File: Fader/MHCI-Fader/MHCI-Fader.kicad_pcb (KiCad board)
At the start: 2 copper layers, 1 part

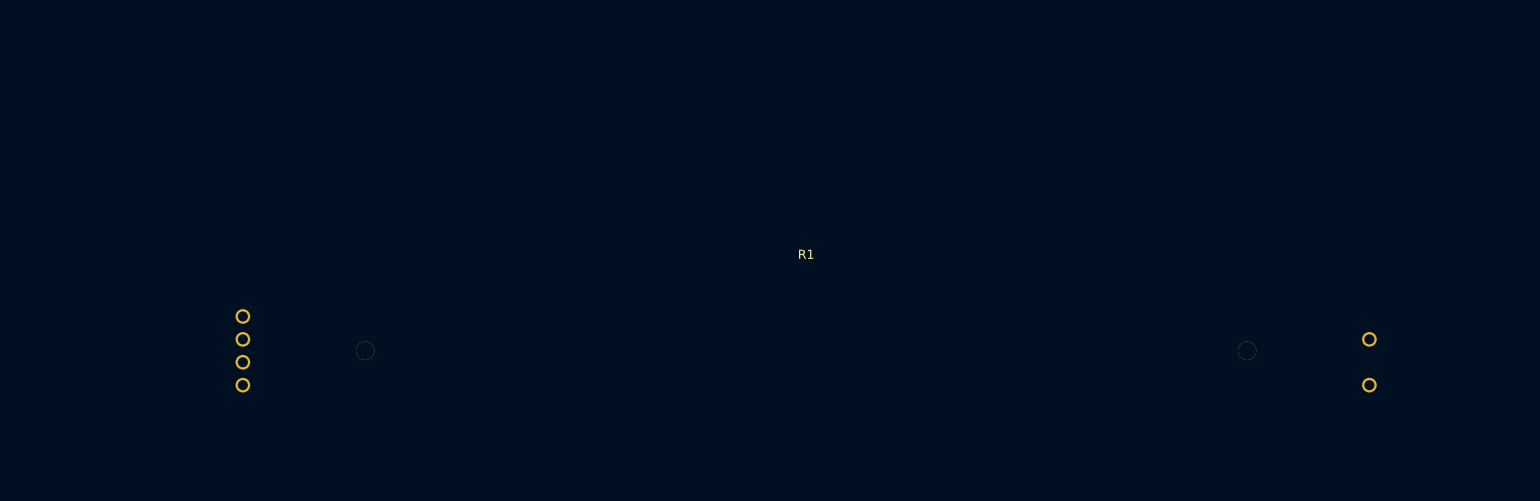
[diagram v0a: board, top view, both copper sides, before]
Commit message: Add all Waveshare footprints
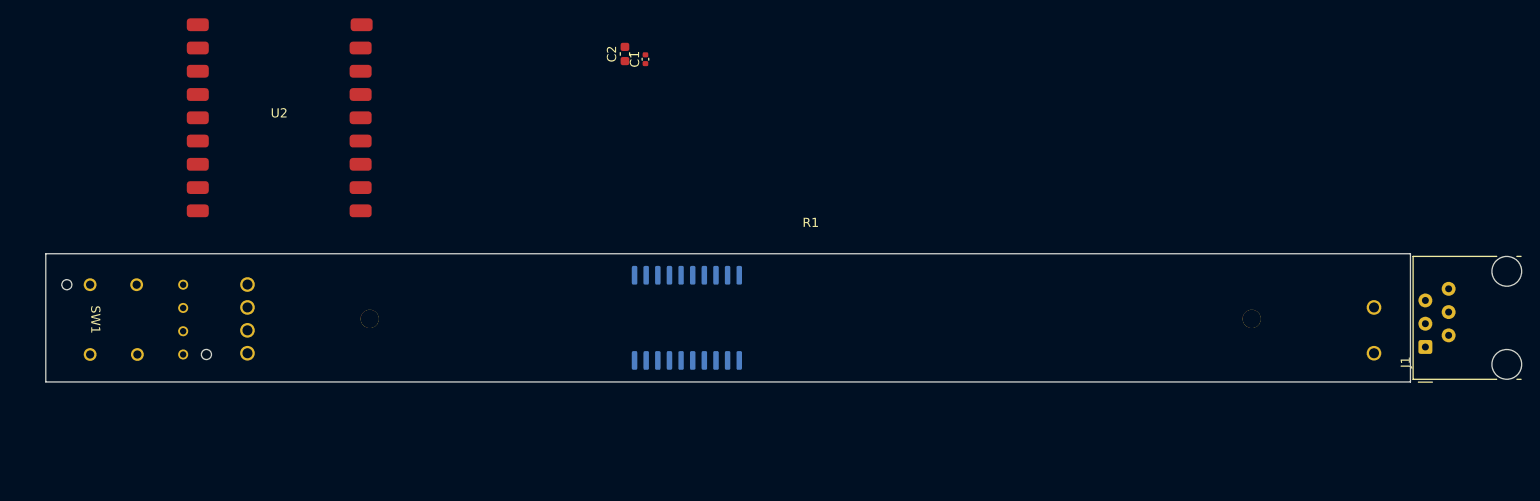
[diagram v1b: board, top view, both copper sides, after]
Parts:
- added C1: 1uF, Capacitor_SMD:C_0402_1005Metric, F.Cu at (128.5, 73.8)
- added C2: 10u, Capacitor_SMD:C_0603_1608Metric, F.Cu at (126.2, 73.2)
- added J1: RJ12, Connector_RJ:RJ12_Amphenol_54601-x06_Horizontal, F.Cu at (213.6, 105.2)
- added SW1: SW_Push_LED, MCHI:SP86N_AB Switch, F.Cu at (72.9, 102.2)
- added U1: ISOW1044, Package_SO:SOIC-20W_7.5x12.8mm_P1.27mm, B.Cu at (133.0, 102.0)
- added U2: ~, MCHI:ESP-32-S3-Zero - SMD, F.Cu at (88.5, 80.2)
- moved R1 3.52 mm to (146.5, 92.1)
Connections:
- R1 pad 1: unconnected-(R1-Pad1) -> +3V3
- R1 pad 2: unconnected-(R1-Pad2) -> Net-(R1-Pad2)
- R1 pad 3: unconnected-(R1-Pad3) -> GND
- R1 pad 4: unconnected-(R1-K-Pad4) -> POT_LED
- R1 pad 5: unconnected-(R1-A-Pad5) -> Net-(R1-A)
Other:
- board outline added: 149 x 14 mm

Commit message: Initial fader schematic
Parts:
- U2: moved to B.Cu
- moved U2 25.7 mm to (102.0, 102.0), turned to 90 degrees
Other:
- board size 149 x 14 mm -> 149 x 20 mm

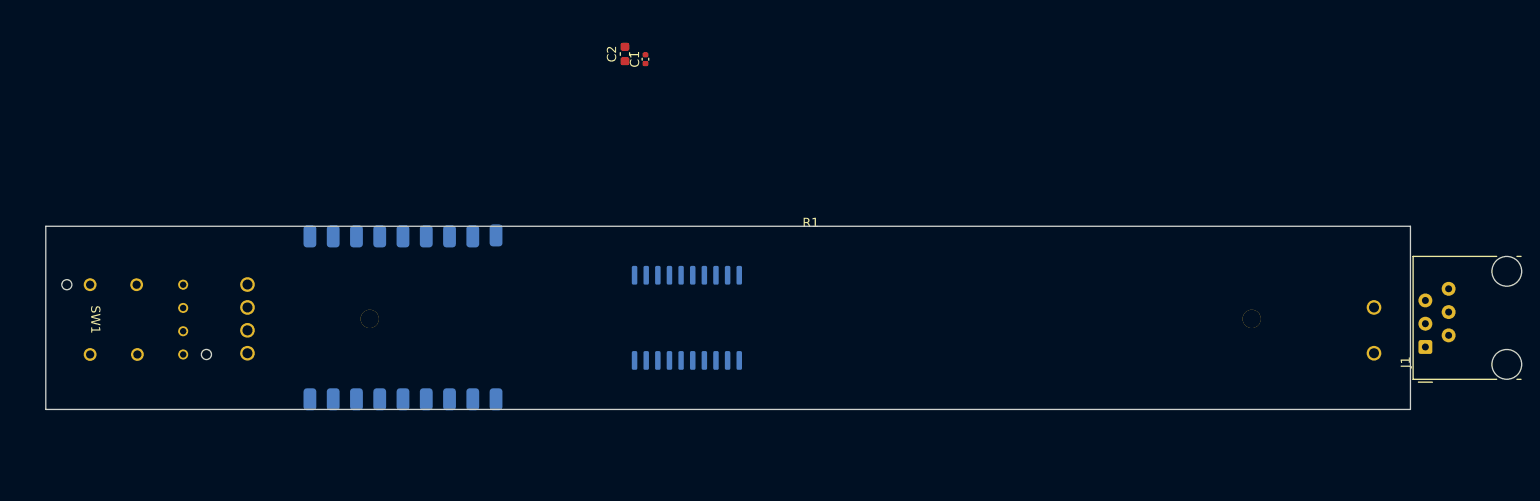
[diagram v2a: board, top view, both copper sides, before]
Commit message: Fader layout complete
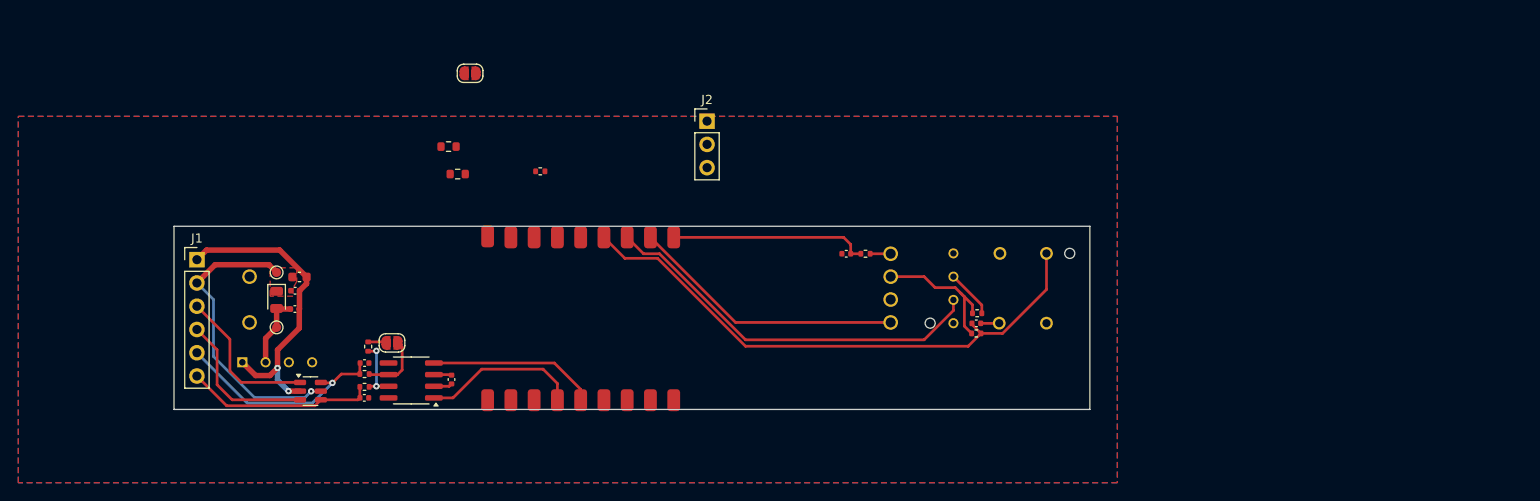
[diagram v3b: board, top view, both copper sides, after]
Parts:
- added C3: 10uF, Capacitor_SMD:C_0603_1608Metric, F.Cu at (90.7, 97.5)
- added C4: 1uF, Capacitor_SMD:C_0402_1005Metric, F.Cu at (90.2, 99.0)
- added C5: 100nF, Capacitor_SMD:C_0402_1005Metric, F.Cu at (90.2, 101.0)
- added C6: 1u, Capacitor_SMD:C_0402_1005Metric, F.Cu at (164.6, 102.6)
- added C7: 100nF, Capacitor_SMD:C_0402_1005Metric, F.Cu at (150.4, 95.0)
- added C8: 30pF, Capacitor_SMD:C_0402_1005Metric, F.Cu at (97.8, 110.7)
- added FB1: FerriteBead, Diode_SMD:D_0805_2012Metric, F.Cu at (88.2, 100.0)
- added J2: Conn_01x03, Connector_PinHeader_2.54mm:PinHeader_1x03_P2.54mm_Vertical, F.Cu at (135.2, 80.5)
- added JP1: Jumper_2_Open, Jumper:SolderJumper-2_P1.3mm_Open_RoundedPad1.0x1.5mm, F.Cu at (109.3, 75.3)
- added JP2: Jumper_2_Open, Jumper:SolderJumper-2_P1.3mm_Open_RoundedPad1.0x1.5mm, F.Cu at (100.8, 104.7)
- added PS1: TBA1-0510, MCHI:CONV_TBA1-0510, B.Cu at (88.3, 108.5)
- added R10: 0R, Resistor_SMD:R_0402_1005Metric, F.Cu at (97.8, 108.1)
- added R2: 220R, Resistor_SMD:R_0402_1005Metric, F.Cu at (152.5, 95.0)
- added R3: 220R, Resistor_SMD:R_0402_1005Metric, F.Cu at (117.0, 86.0)
- added R4: 220R, Resistor_SMD:R_0402_1005Metric, F.Cu at (164.7, 101.5)
- added R5: 4K7, Resistor_SMD:R_0603_1608Metric, F.Cu at (108.0, 86.3)
- added R6: 4K7, Resistor_SMD:R_0603_1608Metric, F.Cu at (107.0, 83.3)
- added R7: 10K, Resistor_SMD:R_0402_1005Metric, F.Cu at (164.6, 103.7)
- added R8: 120R, Resistor_SMD:R_0402_1005Metric, F.Cu at (98.2, 105.1)
- added R9: 0R, Resistor_SMD:R_0402_1005Metric, F.Cu at (97.8, 109.5)
- added TP1: VIN, TestPoint:TestPoint_Pad_D1.0mm, F.Cu at (88.2, 97.0)
- added TP2: 5V, TestPoint:TestPoint_Pad_D1.0mm, F.Cu at (88.2, 103.0)
- added U3: SRV05-4, Package_TO_SOT_SMD:SOT-23-6, F.Cu at (91.9, 110.0)
- C1: value 1uF -> 100nF
- C2: value 10u -> 30pF; footprint Capacitor_SMD:C_0603_1608Metric -> Capacitor_SMD:C_0402_1005Metric
- J1: value RJ12 -> Conn_01x06; footprint Connector_RJ:RJ12_Amphenol_54601-x06_Horizontal -> Connector_PinHeader_2.54mm:PinHeader_1x06_P2.54mm_Vertical
- R1: footprint FaderLibrary:Linear Potentiometer LED 100mm -> FaderLibrary:Linear Potentiometer LED 60mm; moved to B.Cu
- SW1: moved to B.Cu
- U1: value ISOW1044 -> TJA1051T; footprint Package_SO:SOIC-20W_7.5x12.8mm_P1.27mm -> Package_SO:SOIC-8_3.9x4.9mm_P1.27mm; moved to F.Cu
- U2: moved to F.Cu
- moved J1 134.5 mm to (79.5, 95.7), turned to 0 degrees
- moved SW1 94.3 mm to (167.2, 98.8)
- moved C2 44.1 mm to (97.8, 106.9), turned to 180 degrees
- moved C1 40.9 mm to (107.3, 108.7), turned to -90 degrees
- moved U1 30.9 mm to (102.9, 108.8), turned to 180 degrees
- moved R1 26.5 mm to (120.2, 88.8), turned to 180 degrees
- moved U2 19.4 mm to (121.4, 102.1)
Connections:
- C1 pad 1: GND -> +5V
- C1 pad 2: +3V3 -> GND
- C2 pad 1: +3V3 -> GND
- C2 pad 2: GND -> CANL
- J1 pad 1: unconnected-(J1-Pad1) -> Earth
- J1 pad 2: unconnected-(J1-Pad2) -> VIN
- J1 pad 3: unconnected-(J1-Pad3) -> SDA
- J1 pad 4: unconnected-(J1-Pad4) -> SCL
- J1 pad 5: unconnected-(J1-Pad5) -> CANL
- J1 pad 6: unconnected-(J1-Pad6) -> CANH
- SW1 pad 1: unconnected-(SW1-Pad1) -> GND
- SW1 pad 2: unconnected-(SW1-Pad2) -> BUTTON
- U1 pad 1: unconnected-(U1-VIO-Pad1) -> CAN_TX
- U1 pad 2: unconnected-(U1-IN-Pad2) -> GND
- U1 pad 3: unconnected-(U1-TXD-Pad3) -> +5V
- U1 pad 4: unconnected-(U1-STB-Pad4) -> CAN_RX
- U1 pad 6: unconnected-(U1-GNDIO-Pad6) -> /CANH_L
- U1 pad 7: unconnected-(U1-NC-Pad7) -> /CANH_T
- U1 pad 8: unconnected-(U1-EN/FLT-Pad8) -> CAN_S
- U2 pad 1: /ESP_32_GPIO_01 -> CAN_TX
- U2 pad 10: /ESP_32_GPIO_10 -> BUTTON
- U2 pad 2: /ESP_32_GPIO_02 -> CAN_RX
- U2 pad 3: /ESP_32_GPIO_03 -> SCL
- U2 pad 4: /ESP_32_GPIO_04 -> SDA
- U2 pad 5V: +5V -> Net-(JP1-A)
- U2 pad 7: /ESP_32_GPIO_07 -> POT
- U2 pad 8: /ESP_32_GPIO_08 -> POT_LED
- U2 pad 9: /ESP_32_GPIO_09 -> BUTTON_LED
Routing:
- net BUTTON: track 0.00 -> 61.3 mm
- net BUTTON_LED: track 0.00 -> 42.7 mm
- net Earth: track 0.00 -> 33.9 mm, vias 0 -> 2
- net VIN: track 0.00 -> 32.5 mm, vias 0 -> 1
- net POT_LED: track 0.00 -> 30.1 mm
- net CANL: track 0.00 -> 23.9 mm, vias 0 -> 1
- net POT: track 0.00 -> 21.8 mm
- net CANH: track 0.00 -> 20.7 mm
- net CAN_RX: track 0.00 -> 18.4 mm
- net CAN_TX: track 0.00 -> 17.3 mm
- net SDA: track 0.00 -> 16.7 mm
- net SCL: track 0.00 -> 16.7 mm
- net +3V3: track 0.00 -> 16.0 mm
- net +5V: track 0.00 -> 9.87 mm
- net /CANH_L: track 0.00 -> 6.98 mm
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- added copper zone on B.Cu, net GND
- added copper zone on F.Cu, net GND
- added copper zone on F.Cu, net VIN
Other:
- board size 149 x 20 mm -> 100 x 20 mm

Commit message: Merge remote-tracking branch 'origin/main'
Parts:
- moved J2 41.5 mm to (164.5, 110.0), turned to 90 degrees
- moved R3 36.9 mm to (85.2, 104.8), turned to -90 degrees
- moved JP1 29.4 mm to (107.7, 104.7), turned to 180 degrees
- moved R6 19.4 mm to (101.6, 101.9), turned to -90 degrees
- moved R5 16.8 mm to (100.0, 101.1), turned to -90 degrees
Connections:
- J2 pad 1: unconnected-(J2-Pin_1-Pad1) -> DMX+
- J2 pad 2: unconnected-(J2-Pin_2-Pad2) -> DMX-
- J2 pad 3: unconnected-(J2-Pin_3-Pad3) -> GND
- U2 pad 5: /ESP_32_GPIO_05 -> DMX-
- U2 pad 6: /ESP_32_GPIO_06 -> DMX+
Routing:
- net +3V3: track 16.0 -> 125.7 mm, vias 0 -> 3
- net SDA: track 16.7 -> 60.2 mm
- net SCL: track 16.7 -> 57.7 mm
- net DMX-: track 0.00 -> 39.4 mm
- net DMX+: track 0.00 -> 33.3 mm
- net +5V: track 9.87 -> 35.9 mm, vias 0 -> 1
- net Net-(JP1-A): track 0.00 -> 8.45 mm, vias 0 -> 2
- net VIN: track 32.5 -> 34.8 mm
- net CANL: track 23.9 -> 26.0 mm
- net Net-(R1-A): track 0.00 -> 1.81 mm
- net GND: track 4.06 -> 5.56 mm, vias 0 -> 26
- net /CANH_T: track 6.93 -> 6.39 mm
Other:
- outline, holes or cut-outs redrawn

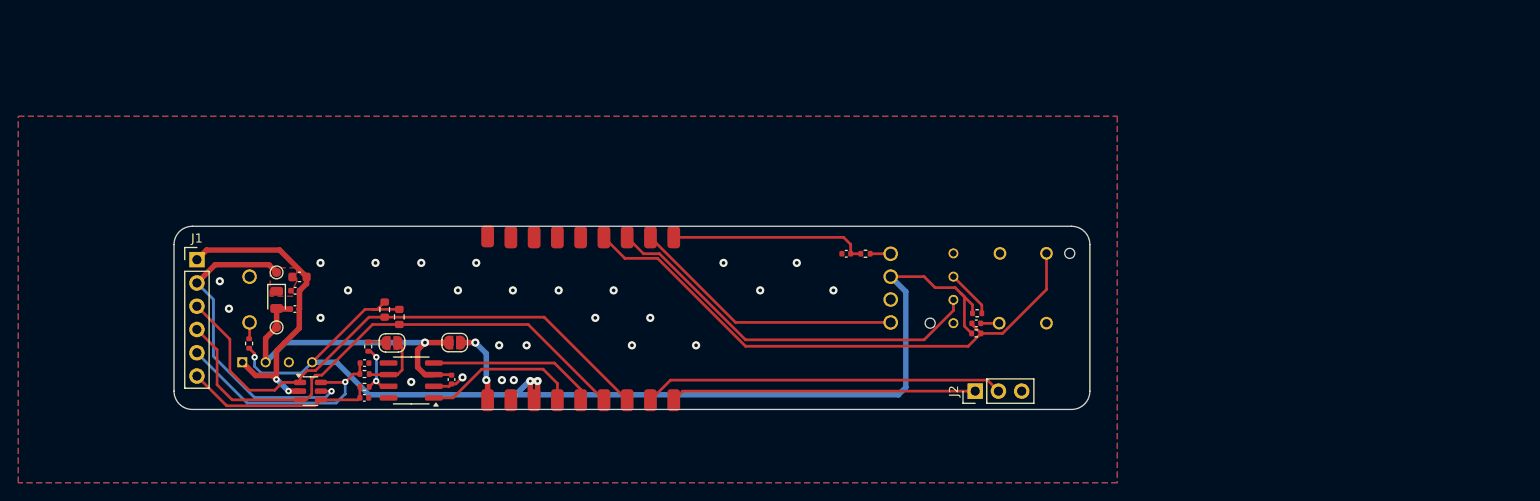
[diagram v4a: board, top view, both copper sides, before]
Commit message: Adjusted fader layout to compact arrangement
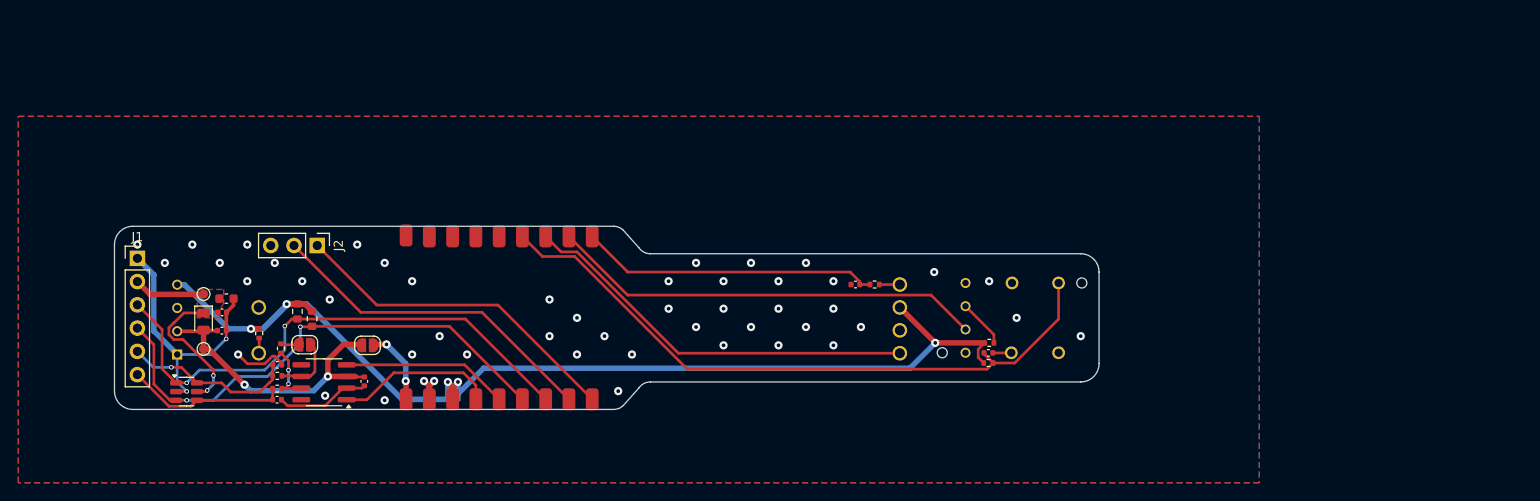
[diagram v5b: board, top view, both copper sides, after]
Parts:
- moved J2 73.6 mm to (92.6, 94.1), turned to -90 degrees
- moved U3 13.5 mm to (78.4, 110.0)
- moved PS1 11.2 mm to (79.0, 102.2), turned to 90 degrees
- moved JP1 9.53 mm to (98.1, 105.0)
- moved C8 9.53 mm to (88.3, 110.9)
- moved R5 9.53 mm to (90.5, 101.3)
- moved R8 9.53 mm to (88.7, 105.3)
- moved U1 9.53 mm to (93.4, 109.0)
- moved C1 9.53 mm to (97.8, 108.9)
- moved C2 9.53 mm to (88.3, 107.1)
- moved JP2 9.53 mm to (91.3, 104.9)
- moved R10 9.53 mm to (88.3, 108.3)
- moved R6 9.53 mm to (92.1, 102.1)
- moved R9 9.53 mm to (88.3, 109.7)
- moved U2 8.90 mm to (112.5, 102.0)
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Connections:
- U2 pad 8: POT_LED -> BUTTON_LED
- U2 pad 9: BUTTON_LED -> POT_LED
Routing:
- net GND: track 5.56 -> 22.7 mm, vias 26 -> 49
- net POT_LED: track 30.1 -> 44.0 mm
- net VIN: track 34.8 -> 23.2 mm, vias 1 -> 2
- net BUTTON: track 61.3 -> 72.3 mm
- net POT: track 21.8 -> 32.7 mm
- net CANL: track 26.0 -> 18.8 mm
- net Earth: track 33.8 -> 28.7 mm
- net BUTTON_LED: track 42.7 -> 47.5 mm
- net DMX+: track 33.3 -> 37.0 mm
- net +3V3: track 125.7 -> 122.7 mm, vias 3 -> 5
- net CANH: track 20.7 -> 17.7 mm
- net DMX-: track 39.4 -> 37.0 mm
- net SCL: track 57.7 -> 55.5 mm, vias 0 -> 2
- net +5V: track 35.9 -> 33.8 mm, vias 1 -> 2
- net SDA: track 60.2 -> 58.7 mm, vias 0 -> 2
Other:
- board size 100 x 20 mm -> 107.5 x 20 mm

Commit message: Fader silkscreen
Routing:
- net GND: vias 49 -> 48
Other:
- board text added: "3V3"
- board text added: "5V"
- board text added: "5V ISO"
- board text added: "CAN"
- board text added: "ESP32-S3 Zero/Tiny"
- board text added: "GND"
- board text added: "H"
- board text added: "L"
- board text added: "RX"
- board text added: "SCL"
- board text added: "SDA"
- board text added: "TERM"
- board text added: "TX"
- board text added: "VIN"
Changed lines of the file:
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@@
 			(at 0 -2.33 360)
 			(layer "F.SilkS")
+			(hide yes)
 			(effects
 				(font
@@
 			(at 0 -2.33 90)
 			(layer "F.SilkS")
+			(hide yes)
 			(effects
 				(font
@@
 		(layer "Edge.Cuts")
 	)
+	(gr_text "5V"
+		(at 102.7 107.7 90)
+		(layer "F.SilkS")
+		(effects
+			(font
+				(size 0.66 0.66)
+				(thickness 0.1)
+			)
+			(justify bottom)
+		)
+	)
+	(gr_text "5V"
+		(at 74.8 98 90)
+		(layer "F.SilkS")
+		(effects
+			(font
+				(size 0.66 0.66)
+				(thickness 0.1)
+			)
+			(justify top)
+		)
+	)
+	(gr_text "TERM"
+		(at 93 104.9 90)
+		(layer "F.SilkS")
+		(effects
+			(font
+				(size 0.66 0.66)
+				(thickness 0.1)
+			)
+			(justify top)
+		)
+	)
+	(gr_text "GND"
+		(at 74.8 95.5 90)
+		(layer "F.SilkS")
+		(effects
+			(font
+				(size 0.66 0.66)
+				(thickness 0.1)
+			)
+			(justify top)
+		)
+	)
+	(gr_text "5V ISO"
+		(at 100.6 104.8 90)
+		(layer "F.SilkS")
+		(effects
+			(font
+				(size 0.66 0.66)
+				(thickness 0.1)
+			)
+			(justify bottom)
+		)
+	)
+	(gr_text "RX"
+		(at 90.1 95.9 90)
+		(layer "F.SilkS")
+		(effects
+			(font
+				(size 0.66 0.66)
+				(thickness 0.1)
+			)
+			(justify right)
+		)
+	)
+	(gr_text "SDA"
+		(at 74.8 100.6 90)
+		(layer "F.SilkS")
+		(effects
+			(font
+				(size 0.66 0.66)
+				(thickness 0.1)
+			)
+			(justify top)
+		)
+	)
+	(gr_text "3V3"
+		(at 77.3 97.6 0)
+		(layer "F.SilkS")
+		(effects
+			(font
+				(size 0.66 0.66)
+				(thickness 0.1)
+			)
+			(justify bottom)
+		)
+	)
+	(gr_text "TX"
+		(at 92.7 95.9 90)
+		(layer "F.SilkS")
+		(effects
+			(font
+				(size 0.66 0.66)
+				(thickness 0.1)
+			)
+			(justify right)
+		)
+	)
+	(gr_text "5V"
+		(at 80.2 107.2 0)
+		(layer "F.SilkS")
+		(effects
+			(font
+				(size 0.66 0.66)
+				(thickness 0.1)
+			)
+			(justify bottom)
+		)
+	)
+	(gr_text "L"
+		(at 74.8 105.6 90)
+		(layer "F.SilkS")
+		(effects
+			(font
+				(size 0.66 0.66)
+				(thickness 0.1)
+			)
+			(justify top)
+		)
+	)
+	(gr_text "GND"
+		(at 87.5 95.9 90)
+		(layer "F.SilkS")
+		(effects
+			(font
+				(size 0.66 0.66)
+				(thickness 0.1)
+			)
+			(justify right)
+		)
+	)
+	(gr_text "ESP32-S3\nZero/Tiny"
+		(at 114.5 102 90)
+		(layer "F.SilkS")
+		(effects
+			(font
+				(size 1.5 1.5)
+				(thickness 0.2)
+			)
+			(justify bottom)
+		)
+	)
+	(gr_text "VIN"
+		(at 80.2 98.3 0)
+		(layer "F.SilkS")
+		(effects
+			(font
+				(size 0.66 0.66)
+				(thickness 0.1)
+			)
+			(justify bottom)
+		)
+	)
+	(gr_text "SCL"
+		(at 74.8 103.1 90)
+		(layer "F.SilkS")
+		(effects
+			(font
+				(size 0.66 0.66)
+				(thickness 0.1)
+			)
+			(justify top)
+		)
+	)
+	(gr_text "CAN"
+		(at 76.4 106.8 90)
+		(layer "F.SilkS")
+		(effects
+			(font
+				(size 0.66 0.66)
+				(thickness 0.1)
+			)
+			(justify bottom)
+		)
+	)
+	(gr_text "H"
+		(at 74.8 108.2 90)
+		(layer "F.SilkS")
+		(effects
+			(font
+				(size 0.66 0.66)
+				(thickness 0.1)
+			)
+			(justify top)
+		)
+	)
 	(segment
 		(start 160.1175 104.73)
@@
 		(size 0.9)
 		(drill 0.4)
-		(layers "F.Cu" "B.Cu")
-		(free yes)
-		(net 2)
-	)
-	(via
-		(at 88 96)
-		(size 0.9)
-		(drill 0.4)

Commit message: Fader silkscreen ATT
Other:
- board text added: "Followspot Fader V1.0"
- board text added: "TT"
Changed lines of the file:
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@@
 		(tags "Through hole pin header THT 1x06 2.54mm single row")
 		(property "Reference" "J1"
-			(at 0 -2.33 360)
+			(at 0 -2.33 0)
 			(layer "F.SilkS")
 			(hide yes)
@@
 		)
 		(property "Value" "Conn_01x06"
-			(at 0 15.03 360)
+			(at 0 15.03 0)
 			(layer "F.Fab")
 			(effects
@@
 		)
 		(fp_text user "${REFERENCE}"
-			(at 0 2.54 360)
+			(at 0 2.54 0)
 			(layer "F.Fab")
 			(effects
@@
 		)
 	)
+	(gr_poly
+		(pts
+			(xy 117.59 111.61) (xy 118.03 110.3) (xy 118.14 110.3) (xy 118.58 111.61) (xy 118.35 111.61) (xy 118.09 110.74)
+			(xy 117.82 111.61)
+		)
+		(stroke
+			(width 0.05)
+			(type solid)
+		)
+		(fill solid)
+		(layer "B.SilkS")
+	)
 	(gr_line
 		(start 126.06066 111.56066)
@@
 		(layer "Edge.Cuts")
 	)
+	(gr_text "TT"
+		(at 116.5 111 0)
+		(layer "B.SilkS")
+		(effects
+			(font
+				(face "Inconsolata")
+				(size 1.5 1.5)
+				(thickness 0.3)
+				(bold yes)
+			)
+			(justify mirror)
+		)
+		(render_cache "TT" 0
+			(polygon
+				(pts
+					(xy 117.146999 111.6225) (xy 117.146999 110.51095) (xy 117.500174 110.51095) (xy 117.500174 110.30945)
+					(xy 116.545795 110.30945) (xy 116.545795 110.51095) (xy 116.917288 110.51095) (xy 116.917288 111.6225)
+				)
+			)
+			(polygon
+				(pts
+					(xy 116.097731 111.6225) (xy 116.097731 110.51095) (xy 116.450906 110.51095) (xy 116.450906 110.30945)
+					(xy 115.496527 110.30945) (xy 115.496527 110.51095) (xy 115.868021 110.51095) (xy 115.868021 111.6225)
+				)
+			)
+		)
+	)
+	(gr_text "Followspot Fader V1.0"
+		(at 114.75 94 0)
+		(layer "B.SilkS")
+		(effects
+			(font
+				(size 1 1)
+				(thickness 0.15)
+			)
+			(justify bottom mirror)
+		)
+	)
 	(gr_text "5V"
 		(at 102.7 107.7 90)
@@
 		)
 	)
+	(gr_text "Followspot\nFader\nV1.0"
+		(at 142.75 102 90)
+		(layer "F.SilkS")
+		(effects
+			(font
+				(size 1 1)
+				(thickness 0.15)
+			)
+			(justify bottom)
+		)
+	)
